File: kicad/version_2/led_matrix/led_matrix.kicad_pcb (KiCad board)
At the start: 2 copper layers, 220 x 172 mm, 45 parts, among them Q1 IRF540N, Q2 IRF540N, Q3 IRF540N, Q4 IRF540N, Q5 IRF540N, Q6 IRF540N, Q7 IRF540N, Q9 IRF540N, SW1 SW_DIP_x01

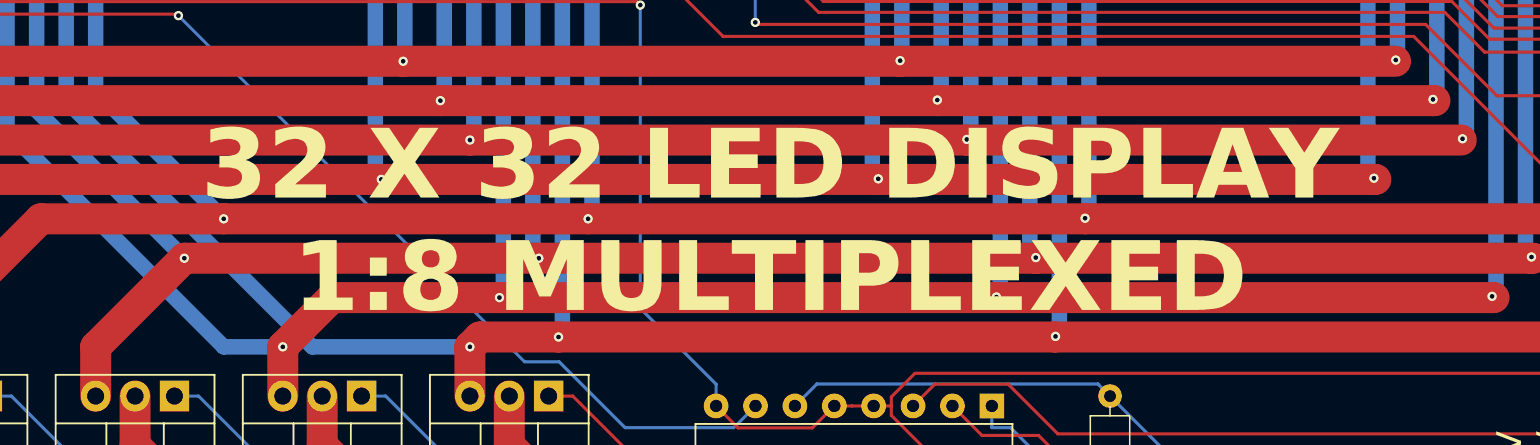
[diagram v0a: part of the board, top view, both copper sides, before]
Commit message: Tetris program draw-shape and init-next-shape-from-storage functions work
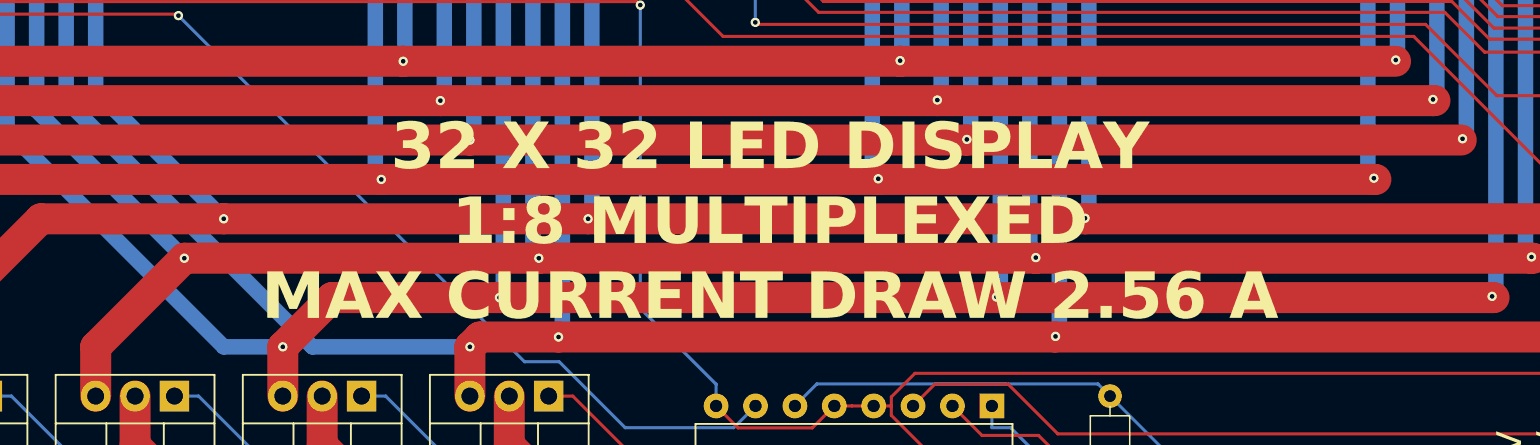
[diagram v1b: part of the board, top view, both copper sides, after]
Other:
- board text added: "32 X 32 LED DISPLAY 1:8 MULTIPLEXED MAX CURRENT DRAW 2.56 A"
- board text removed: "32 X 32 LED DISPLAY 1:8 MULTIPLEXED"
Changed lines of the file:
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@@
 		(layer "Edge.Cuts")
 	)
-	(gr_text "32 X 32 LED DISPLAY\n1:8 MULTIPLEXED"
+	(gr_text "32 X 32 LED DISPLAY\n1:8 MULTIPLEXED\nMAX CURRENT DRAW 2.56 A"
 		(at 521 261.25 0)
 		(layer "F.SilkS")
 		(effects
 			(font
-				(size 4.5 4.5)
-				(thickness 0.9)
+				(size 3 3)
+				(thickness 0.6)
 				(bold yes)
 			)
